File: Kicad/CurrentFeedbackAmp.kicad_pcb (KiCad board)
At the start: 2 copper layers, 200 x 100 mm, 123 parts, among them J1 Test_Etapa_3_Inf, J10 Protecc_Sup_In1, J11 Protecc_Inf_In1, J12 Protecc_Sup_In2, J13 Test_Etapa_3_Inf, J14 Entrada, J15 Salida masa2, J16 Salida tierra, J17 Salida senal, J2 Test_Realim_Out, J3 Salida masa1, J4 Protecc_Sup_Out, J5 Protecc_Inf_Out, J6 Conector Vcc, J7 Conector Vdd, J8 Test_Etapa_3_Inf, J9 Test_Etapa_3_Sup, Q1 TIP42C, Q10 BC858, Q11 BC848, Q12 BC858, Q13 BC559, Q14 BC559, Q15 BC559, Q16 BC549, Q17 BC549, Q18 BC549, Q19 BC559, Q2 BD135, Q20 BC549, Q21 BC559, Q22 BC549, Q23 BC848, Q24 BD136, Q25 BC858, Q26 BC848, Q27 BC848, Q28 BC848, Q29 BC858, Q3 BD136, Q30 BC858, Q31 BC848, Q32 BC858, Q33 BD135, Q34 TIP41C, Q35 BC858, Q36 BC848, Q37 BC848, Q38 BC848, Q4 BC848, Q40 BC858, Q41 BC858, Q5 BC848, Q6 BC858, Q7 BC858, Q8 BC848, Q9 BC858, U1 LM7812_TO220, U2 TL082, U3 LM7912_TO220, U4 LM7805_TO220, U5 LM7905_TO220

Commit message: Primer intento de unir la ultima conexion
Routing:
- net Net-(Q23-Pad1): track 0.00 -> 139.7 mm, vias 0 -> 6
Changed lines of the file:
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@@
     (thickness 1.6)
     (drawings 6)
-    (tracks 757)
+    (tracks 784)
     (zones 0)
     (modules 123)
@@
   (segment (start 159.385 49.53) (end 152.81 49.53) (width 1) (layer F.Cu) (net 49))
   (segment (start 152.81 49.53) (end 152.715 49.435) (width 1) (layer F.Cu) (net 49))
+  (segment (start 151.765 51.435) (end 148.935 51.435) (width 1) (layer F.Cu) (net 50))
+  (segment (start 148.935 51.435) (end 147.5 50) (width 1) (layer F.Cu) (net 50))
+  (segment (start 147.5 50) (end 147.5 47.5) (width 1) (layer F.Cu) (net 50))
+  (segment (start 147.5 47.5) (end 150 47.5) (width 1) (layer F.Cu) (net 50))
+  (segment (start 150 47.5) (end 152 45.5) (width 1) (layer F.Cu) (net 50))
+  (via (at 152 45.5) (size 0.6) (drill 0.4) (layers F.Cu B.Cu) (net 50))
+  (segment (start 152 31.5) (end 152 45.5) (width 1) (layer B.Cu) (net 50))
+  (segment (start 147 26.5) (end 152 31.5) (width 1) (layer F.Cu) (net 50))
+  (via (at 152 31.5) (size 0.6) (drill 0.4) (layers F.Cu B.Cu) (net 50))
+  (segment (start 142 26.5) (end 147 26.5) (width 1) (layer F.Cu) (net 50))
+  (segment (start 139 26.5) (end 142 26.5) (width 1) (layer B.Cu) (net 50))
+  (via (at 142 26.5) (size 0.6) (drill 0.4) (layers F.Cu B.Cu) (net 50))
+  (segment (start 135 22.5) (end 139 26.5) (width 1) (layer B.Cu) (net 50))
+  (segment (start 133 22.5) (end 135 22.5) (width 1) (layer B.Cu) (net 50))
+  (segment (start 92.60247 16.60247) (end 98.5 22.5) (width 1) (layer F.Cu) (net 50))
+  (segment (start 98.5 22.5) (end 133 22.5) (width 1) (layer F.Cu) (net 50))
+  (via (at 133 22.5) (size 0.6) (drill 0.4) (layers F.Cu B.Cu) (net 50))
+  (segment (start 73 21.5) (end 77.89753 16.60247) (width 1) (layer F.Cu) (net 50))
+  (segment (start 77.89753 16.60247) (end 92.60247 16.60247) (width 1) (layer F.Cu) (net 50))
+  (via (at 73 21.5) (size 0.6) (drill 0.4) (layers F.Cu B.Cu) (net 50))
+  (segment (start 63 31.5) (end 73 21.5) (width 1) (layer B.Cu) (net 50))
+  (segment (start 62 31.5) (end 63 31.5) (width 1) (layer B.Cu) (net 50))
+  (segment (start 62 38) (end 62 31.5) (width 1) (layer B.Cu) (net 50))
+  (segment (start 59.55 38) (end 62 38) (width 1) (layer F.Cu) (net 50))
+  (via (at 62 38) (size 0.6) (drill 0.4) (layers F.Cu B.Cu) (net 50))
+  (segment (start 57.88 37.78) (end 59.33 37.78) (width 1) (layer F.Cu) (net 50))
+  (segment (start 59.33 37.78) (end 59.55 38) (width 1) (layer F.Cu) (net 50))
   (segment (start 46.67 46.895) (end 44.77 46.895) (width 1) (layer F.Cu) (net 51))
   (segment (start 44.31 47.355) (end 44.77 46.895) (width 1) (layer F.Cu) (net 51))

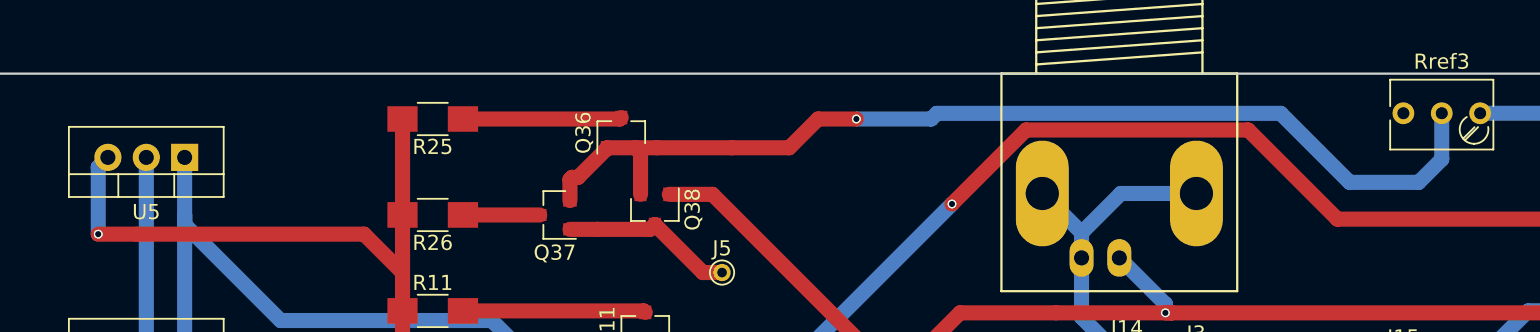
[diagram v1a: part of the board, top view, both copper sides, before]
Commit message: Mejoras en dos caminos para evitar que se solapen con otras pistas
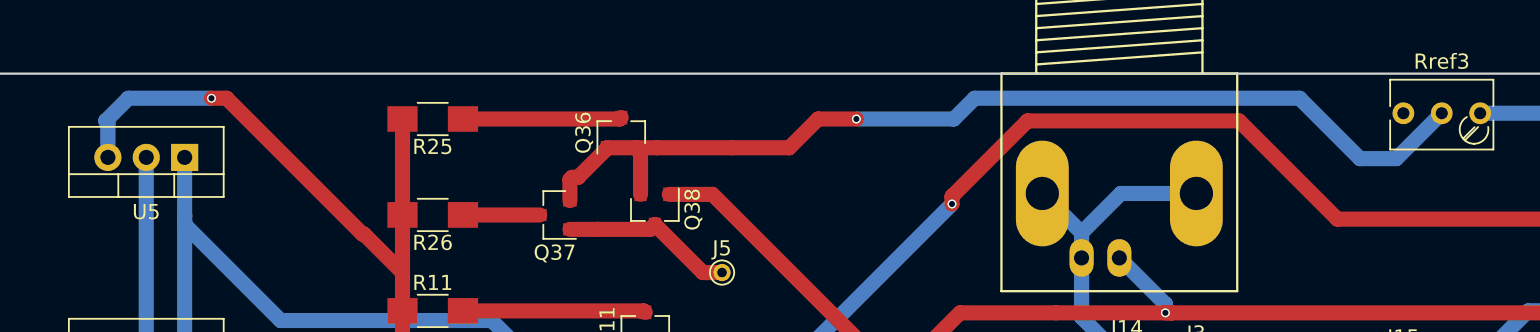
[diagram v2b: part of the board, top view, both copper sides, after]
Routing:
- net Net-(Q36-Pad1): track 69.7 -> 67.5 mm
- net Vdd5: track 58.0 -> 58.9 mm
- net Net-(Q23-Pad1): track 139.7 -> 140.5 mm

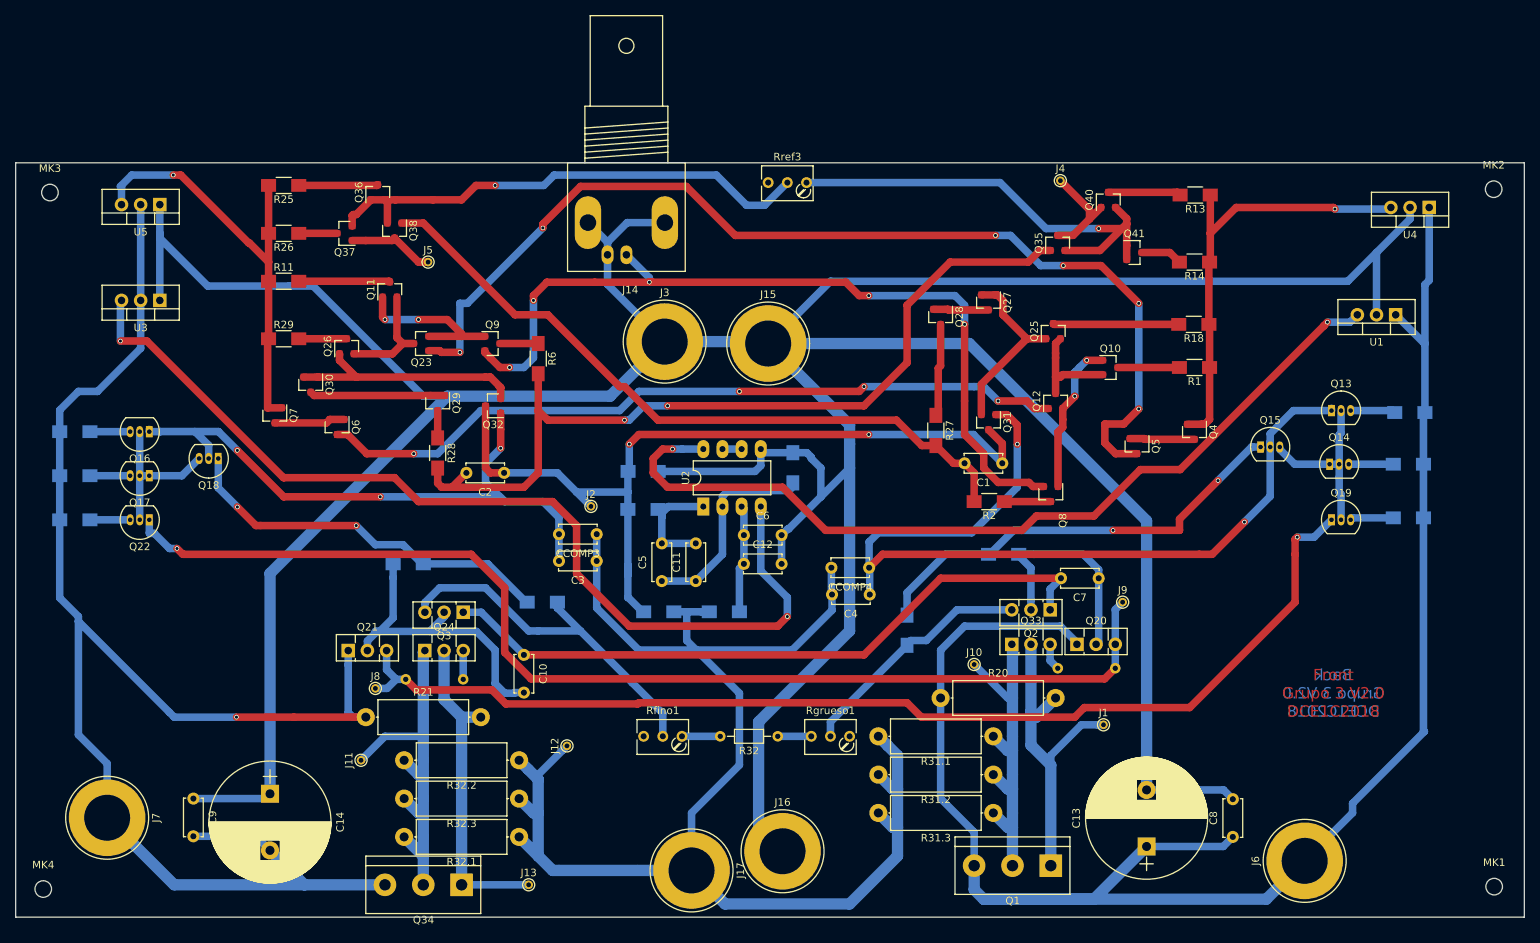
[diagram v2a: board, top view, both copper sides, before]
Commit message: Se agregan textos para saber mejor los puntos importantes
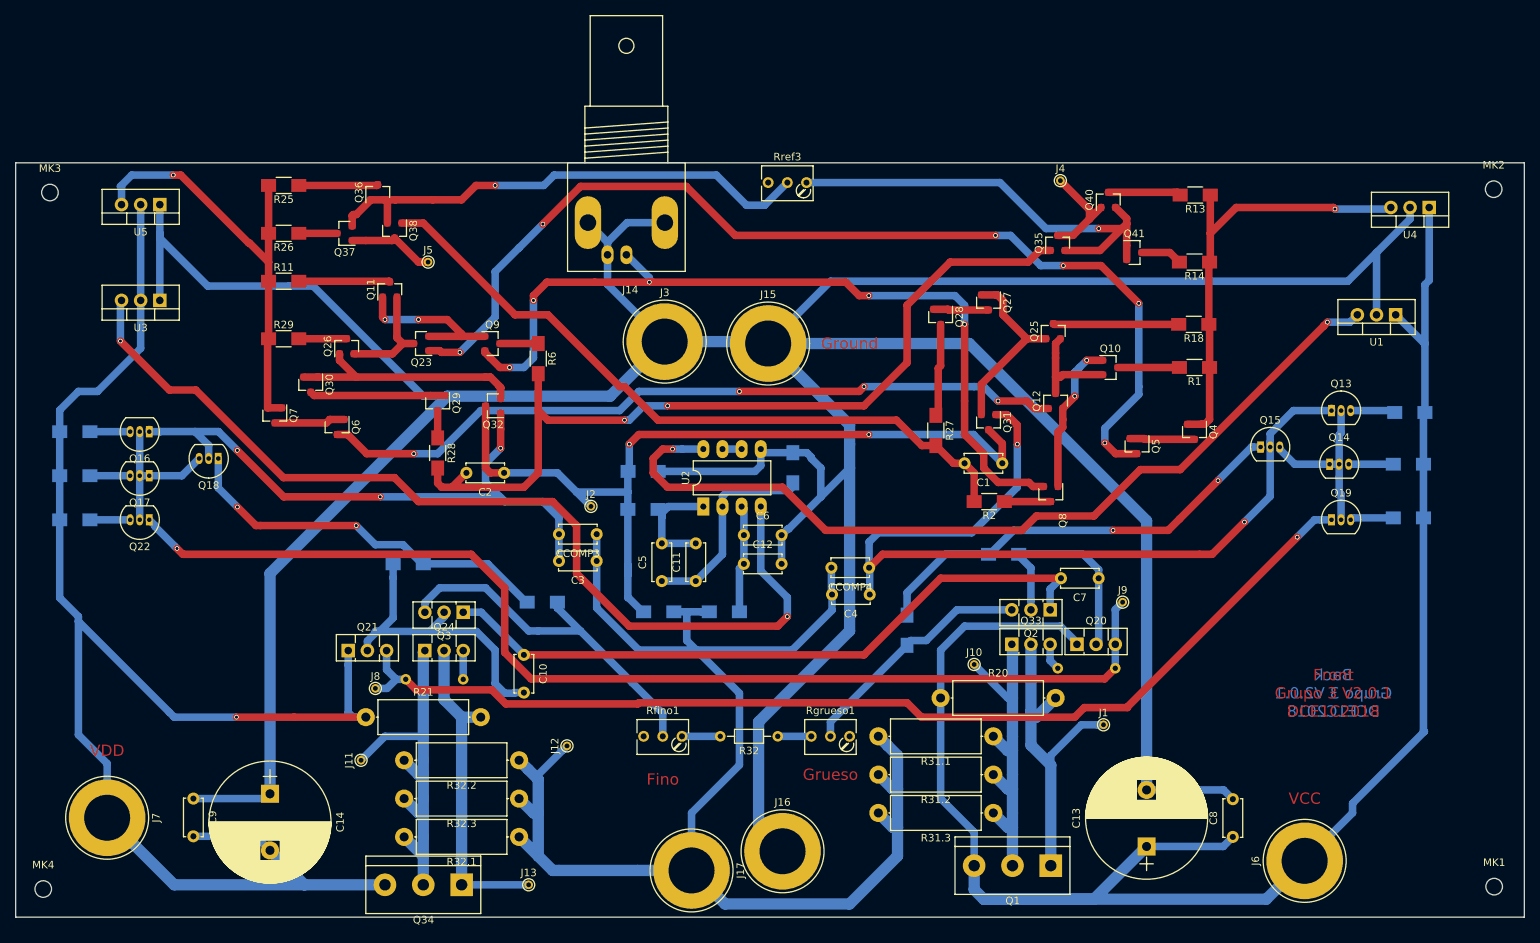
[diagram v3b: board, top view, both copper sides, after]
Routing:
- net Net-(J8-Pad1): track 149.5 -> 144.7 mm
- net Net-(Q23-Pad1): track 140.5 -> 138.5 mm
- net Net-(J9-Pad1): track 152.6 -> 151.6 mm
- net Net-(Q15-Pad1): track 59.4 -> 58.5 mm
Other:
- board text added: "Back Grupo 3 V2.0.1 DCE1C2018"
- board text added: "Fino"
- board text added: "Front Grupo 3 V2.0.1 DCE1C2018"
- board text added: "Ground"
- board text added: "Grueso"
- board text added: "VCC"
- board text added: "VDD"
- board text removed: "Back Grupo 3 V2.0 DCE1C2018"
- board text removed: "Front Grupo 3 V2.0 DCE1C2018"

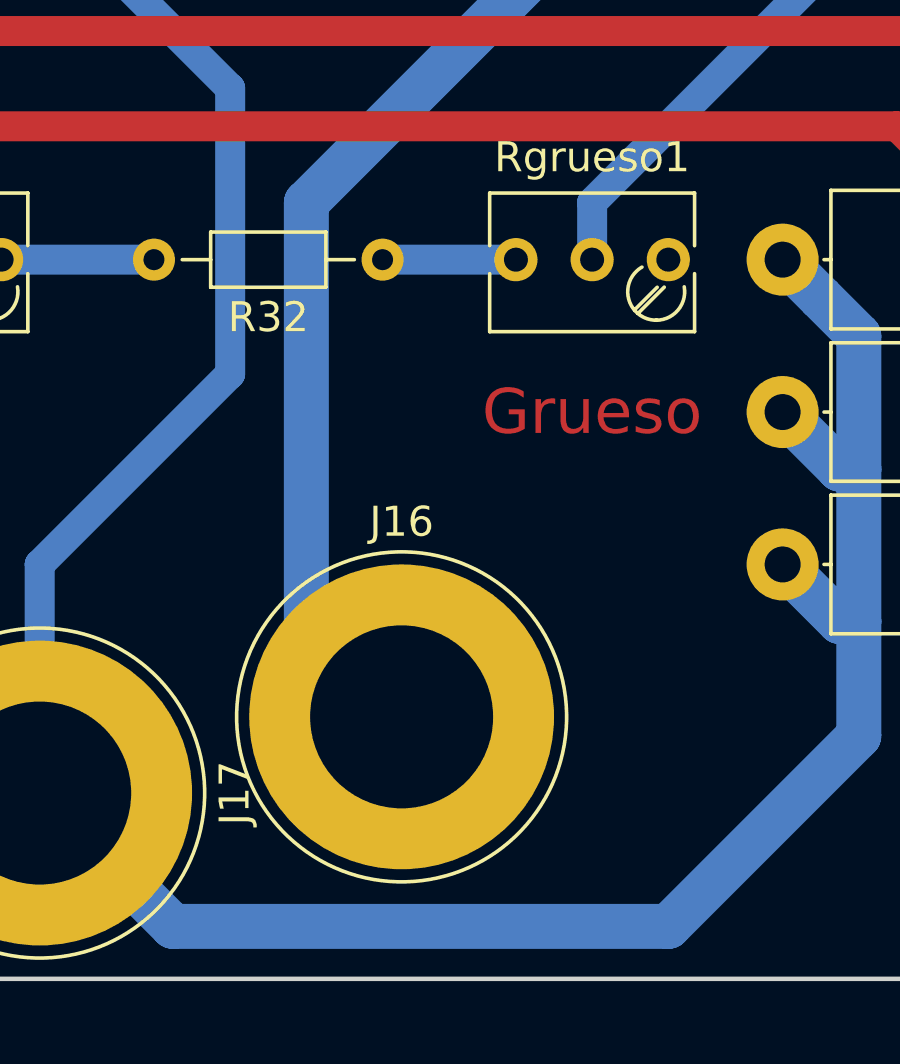
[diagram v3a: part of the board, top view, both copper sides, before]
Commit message: Mayor separacion entre J16 y J17 por seguridad y reactive las diferentes capas
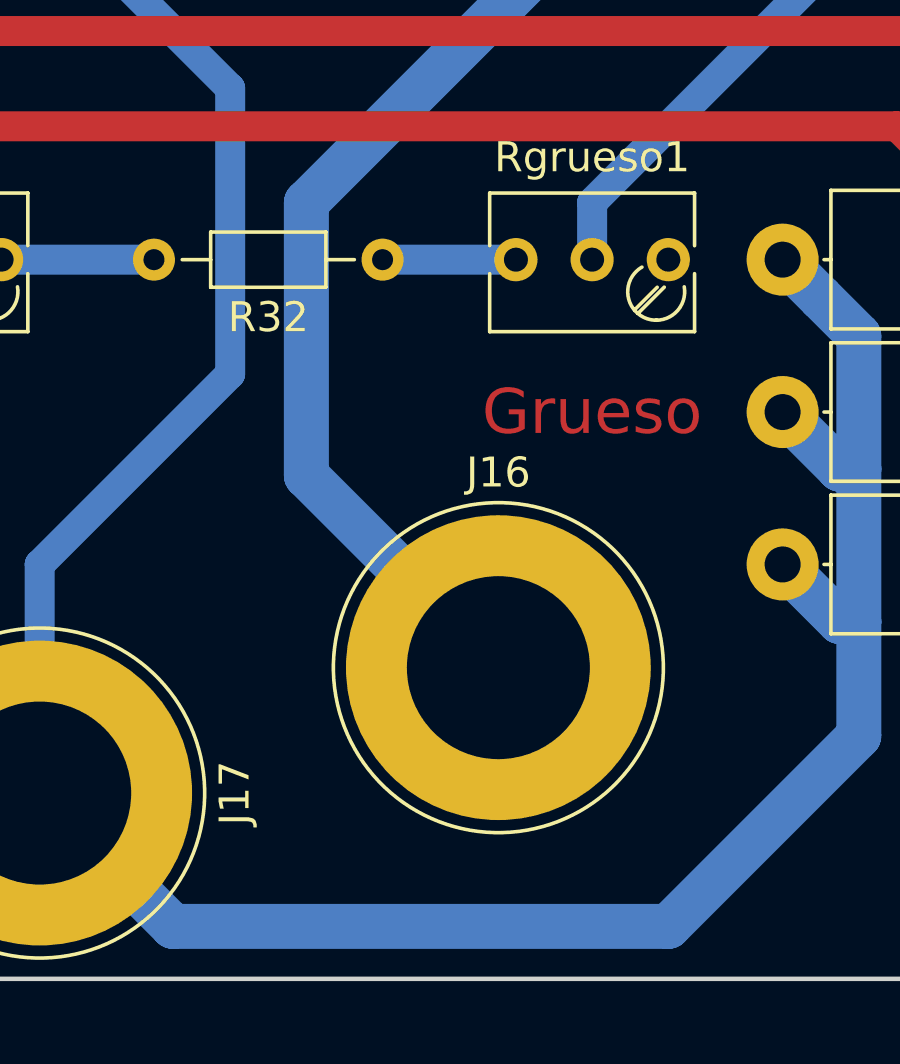
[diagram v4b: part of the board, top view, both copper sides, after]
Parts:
- moved J16 3.62 mm to (108.0, 102.5)
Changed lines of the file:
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@@
     (links 203)
     (no_connects 0)
-    (area 3.036599 12.797799 203.186601 112.947801)
+    (area 1.164338 -6.909481 204.715363 114.31)
     (thickness 1.6)
     (drawings 11)
@@
     (0 F.Cu signal)
     (31 B.Cu signal)
-    (32 B.Adhes user hide)
-    (33 F.Adhes user hide)
-    (34 B.Paste user hide)
-    (35 F.Paste user hide)
-    (36 B.SilkS user hide)
-    (37 F.SilkS user hide)
-    (38 B.Mask user hide)
-    (39 F.Mask user hide)
-    (40 Dwgs.User user hide)
-    (41 Cmts.User user hide)
-    (42 Eco1.User user hide)
-    (43 Eco2.User user hide)
-    (44 Edge.Cuts user hide)
-    (45 Margin user hide)
-    (46 B.CrtYd user hide)
-    (47 F.CrtYd user hide)
-    (48 B.Fab user hide)
-    (49 F.Fab user hide)
+    (32 B.Adhes user)
+    (33 F.Adhes user)
+    (34 B.Paste user)
+    (35 F.Paste user)
+    (36 B.SilkS user)
+    (37 F.SilkS user)
+    (38 B.Mask user)
+    (39 F.Mask user)
+    (40 Dwgs.User user)
+    (41 Cmts.User user)
+    (42 Eco1.User user)
+    (43 Eco2.User user)
+    (44 Edge.Cuts user)
+    (45 Margin user)
+    (46 B.CrtYd user)
+    (47 F.CrtYd user)
+    (48 B.Fab user)
+    (49 F.Fab user)
   )
   (setup
-    (last_trace_width 1)
+    (last_trace_width 1.5)
     (user_trace_width 0.25)
     (user_trace_width 1)
@@
     (solder_mask_min_width 0.25)
     (aux_axis_origin 4.445 5.08)
-    (visible_elements 7FFC0001)
+    (visible_elements 7FFFEFFF)
     (pcbplotparams
       (layerselection 0x01000_80000001)
@@
   )
   (module Connectors:Banana_Jack_1Pin (layer F.Cu)
-    (at 104.775 104.14)
+    (at 108 102.5)
     (descr "Single banana socket, footprint - 6mm drill")
     (tags "banana socket")
@@
   (segment (start 99.649934 58.74338) (end 99.349934 58.44338) (width 1) (layer B.Cu) (net 5))
   (segment (start 99.649934 62.23) (end 99.649934 58.74338) (width 1) (layer B.Cu) (net 5))
+  (segment (start 108 102.5) (end 101.6 96.1) (width 1.5) (layer B.Cu) (net 6))
+  (segment (start 101.6 96.1) (end 101.6 86.995) (width 1.5) (layer B.Cu) (net 6))
   (segment (start 42.545 29.21) (end 57.15 43.815) (width 1) (layer B.Cu) (net 6))
   (segment (start 57.15 43.815) (end 60.325 43.815) (width 1) (layer B.Cu) (net 6))
@@
   (segment (start 113.665 47.625) (end 102.87 36.83) (width 1.5) (layer B.Cu) (net 6))
   (segment (start 101.6 86.995) (end 113.665 74.93) (width 1.5) (layer B.Cu) (net 6))
-  (segment (start 104.775 104.14) (end 101.6 100.965) (width 1.5) (layer B.Cu) (net 6))
-  (segment (start 101.6 100.965) (end 101.6 86.995) (width 1.5) (layer B.Cu) (net 6))
   (segment (start 163.235 96.005) (end 164.465 97.235) (width 1) (layer B.Cu) (net 6))
   (segment (start 153.035 96.005) (end 163.235 96.005) (width 1) (layer B.Cu) (net 6))
